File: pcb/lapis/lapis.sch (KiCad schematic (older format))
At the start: 0 parts

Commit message: 基板修正途中　ソフト動作確認まで
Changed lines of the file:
@@
 $EndDescr
 $Sheet
-S 2000 1500 1600 1350
+S 8050 2900 800  650
+U 5FA81E9C
+F0 "IMU" 50
+F1 "ICM-20602.sch" 50
+F2 "IMU_MISO" O L 8050 3450 50
+F3 "IMU_CS" I L 8050 3000 50
+F4 "IMU_MOSI" I L 8050 3300 50
+F5 "IMU_SCK" I L 8050 3150 50
+$EndSheet
+$Sheet
+S 1850 3600 850  200
+U 5FA82034
+F0 "WALL_LED_LFRS" 50
+F1 "wall_led.sch" 50
+F2 "LED_PWM" I R 2700 3700 50
+$EndSheet
+$Sheet
+S 1850 4650 900  200
+U 5FA821A9
+F0 "WALL_SENSOR_RS" 50
+F1 "wall_sensor.sch" 50
+F2 "WALLSENSOR_ADC" O R 2750 4750 50
+$EndSheet
+$Sheet
+S 1850 5100 900  200
+U 5FA82203
+F0 "WALL_SENSOR_RF" 50
+F1 "wall_sensor.sch" 50
+F2 "WALLSENSOR_ADC" O R 2750 5200 50
+$EndSheet
+$Sheet
+S 8050 1800 800  700
+U 5FA81F75
+F0 "MOTOR_DRIVE" 50
+F1 "DRV8835.sch" 50
+F2 "MR_PWM" I L 8050 2100 50
+F3 "ML_PWM" I L 8050 2250 50
+F4 "ML_EN" I L 8050 2400 50
+F5 "MR_EN" I L 8050 1950 50
+$EndSheet
+$Sheet
+S 1850 5550 900  200
+U 5FA82246
+F0 "WALL_SENSOR_LF" 50
+F1 "wall_sensor.sch" 50
+F2 "WALLSENSOR_ADC" O R 2750 5650 50
+$EndSheet
+$Sheet
+S 1850 6000 900  200
+U 5FA82233
+F0 "WALL_SENSOR_LS" 50
+F1 "wall_sensor.sch" 50
+F2 "WALLSENSOR_ADC" O R 2750 6100 50
+$EndSheet
+$Sheet
+S 2050 1500 600  200
 U 5FA819E2
 F0 "POWER" 50
 F1 "power.sch" 50
-$EndSheet
-$Sheet
-S 4200 1500 1450 1350
-U 5FA81D59
-F0 "CPU" 50
-F1 "STM32F405RGT.sch" 50
-$EndSheet
-$Sheet
-S 6150 1500 1450 1350
-U 5FA81E9C
-F0 "IMU" 50
-F1 "MPU6500.sch" 50
-$EndSheet
-$Sheet
-S -2650 1100 1600 1300
-U 5FA82034
-F0 "WALL_LED_LFRS" 50
-F1 "wall_led.sch" 50
-$EndSheet
-$Sheet
-S -2600 3850 1150 1250
+F2 "AD_BATT" O R 2650 1600 50
+$EndSheet
+$Sheet
+S 1850 4000 850  200
 U 5FA82132
 F0 "WALL_LED_LSRF" 50
 F1 "wall_led.sch" 50
-$EndSheet
-$Sheet
-S -4600 7350 1400 1300
+F2 "LED_PWM" I R 2700 4100 50
+$EndSheet
+$Sheet
+S 8050 4150 1000 650
 U 5FA82159
 F0 "MOTOR_ENCODER_R" 50
 F1 "AS5047P.sch" 50
-$EndSheet
-$Sheet
-S -4250 5150 1400 1400
-U 5FA821A9
-F0 "WALL_SENSOR_RS" 50
-F1 "wall_sensor.sch" 50
-$EndSheet
-$Sheet
-S -2250 7400 1250 1350
-U 5FA82203
-F0 "WALL_SENSOR_RF" 50
-F1 "wall_sensor.sch" 50
-$EndSheet
-$Sheet
-S -2150 5550 1400 1000
+F2 "ENC_CS" I L 8050 4250 50
+F3 "ENC_SCK" I L 8050 4400 50
+F4 "ENC_MISO" O L 8050 4700 50
+F5 "ENC_MOSI" I L 8050 4550 50
+$EndSheet
+$Sheet
+S 8050 5250 1000 650
 U 5FA82269
 F0 "MOTOR_ENCODER_L" 50
 F1 "AS5047P.sch" 50
-$EndSheet
-$Sheet
-S 8000 1500 1400 1350
-U 5FA81F75
-F0 "MOTOR_DRIVE" 50
-F1 "DRV8835.sch" 50
-$EndSheet
-$Sheet
-S -2500 2850 850  650
-U 5FA82246
-F0 "WALL_SENSOR_LF" 50
-F1 "wall_sensor.sch" 50
-$EndSheet
-$Sheet
-S -4300 1150 750  650
-U 5FA82233
-F0 "WALL_SENSOR_LS" 50
-F1 "wall_sensor.sch" 50
-$EndSheet
-$Sheet
-S 1500 3850 1500 1600
-U 5FA82AB3
-F0 "INDICATOR" 50
-F1 "indicator.sch" 50
+F2 "ENC_CS" I L 8050 5350 50
+F3 "ENC_SCK" I L 8050 5500 50
+F4 "ENC_MISO" O L 8050 5800 50
+F5 "ENC_MOSI" I L 8050 5650 50
+$EndSheet
+Wire Wire Line
+	2650 1600 4000 1600
+Wire Wire Line
+	2650 2450 4000 2450
+Wire Wire Line
+	2650 2550 4000 2550
+Wire Wire Line
+	4000 2700 2650 2700
+Wire Wire Line
+	2650 2850 4000 2850
+Wire Wire Line
+	4000 2950 2650 2950
+Wire Wire Line
+	2650 3050 4000 3050
+Wire Wire Line
+	4000 3150 2650 3150
+Wire Wire Line
+	4000 3700 2700 3700
+Wire Wire Line
+	2700 4100 4000 4100
+Wire Wire Line
+	4000 4750 2750 4750
+Wire Wire Line
+	2750 5200 4000 5200
+Wire Wire Line
+	4000 5650 2750 5650
+Wire Wire Line
+	2750 6100 4000 6100
+Wire Wire Line
+	8050 1950 7100 1950
+Wire Wire Line
+	8050 2100 7100 2100
+Wire Wire Line
+	7100 2250 8050 2250
+Wire Wire Line
+	8050 2400 7100 2400
+Wire Wire Line
+	7100 3000 8050 3000
+Wire Wire Line
+	8050 3150 7100 3150
+Wire Wire Line
+	7100 3300 8050 3300
+Wire Wire Line
+	7100 3450 8050 3450
+Wire Wire Line
+	8050 4250 7100 4250
+Wire Wire Line
+	7100 4400 7850 4400
+Wire Wire Line
+	8050 4550 7700 4550
+Wire Wire Line
+	7100 4700 7550 4700
+Wire Wire Line
+	8050 5350 7100 5350
+Wire Wire Line
+	7850 4400 7850 5500
+Wire Wire Line
+	7850 5500 8050 5500
+Connection ~ 7850 4400
+Wire Wire Line
+	7850 4400 8050 4400
+Wire Wire Line
+	7700 4550 7700 5650
+Wire Wire Line
+	7700 5650 8050 5650
+Connection ~ 7700 4550
+Wire Wire Line
+	7700 4550 7100 4550
+Wire Wire Line
+	7550 4700 7550 5800
+Wire Wire Line
+	7550 5800 8050 5800
+Connection ~ 7550 4700
+Wire Wire Line
+	7550 4700 8050 4700
+Wire Wire Line
+	2650 2300 4000 2300
+$Sheet
+S 4000 1450 3100 4800
+U 5FA81D59
+F0 "CPU" 50
+F1 "STM32F411CEU.sch" 50
+F2 "LED_LFRS" O L 4000 3700 50
+F3 "LED_LSRF" O L 4000 4100 50
+F4 "MR_PWM" O R 7100 2100 50
+F5 "MR_EN" O R 7100 1950 50
+F6 "ML_PWM" O R 7100 2250 50
+F7 "ML_EN" O R 7100 2400 50
+F8 "ENC_SCK" O R 7100 4400 50
+F9 "ENC_CS_R" O R 7100 4250 50
+F10 "ENC_CS_L" O R 7100 5350 50
+F11 "ENC_MISO" I R 7100 4700 50
+F12 "ENC_MOSI" O R 7100 4550 50
+F13 "WALLSENSOR_RS" I L 4000 4750 50
+F14 "WALLSENSOR_RF" I L 4000 5200 50
+F15 "WALLSENSOR_LF" I L 4000 5650 50
+F16 "WALLSENSOR_LS" I L 4000 6100 50
+F17 "BATTERY" I L 4000 1600 50
+F18 "IMU_SCK" O R 7100 3150 50
+F19 "IMU_MISO" I R 7100 3450 50
+F20 "IMU_MOSI" O R 7100 3300 50
+F21 "IMU_CS" O R 7100 3000 50
+F22 "SW" I L 4000 2700 50
+F23 "LED1" O L 4000 2950 50
+F24 "LED2" O L 4000 3050 50
+F25 "LED3" O L 4000 3150 50
+F26 "RX" I L 4000 2550 50
+F27 "SPEAKER" O L 4000 2300 50
+F28 "TX" O L 4000 2450 50
+F29 "LED0" O L 4000 2850 50
+$EndSheet
+$Sheet
+S 2100 2200 550  1050
+U 603AF16B
+F0 "UI" 50
+F1 "UI.sch" 50
+F2 "LED1" I R 2650 2950 50
+F3 "LED2" I R 2650 3050 50
+F4 "LED3" I R 2650 3150 50
+F5 "LED0" I R 2650 2850 50
+F6 "SW" O R 2650 2700 50
+F7 "SPEAKER" I R 2650 2300 50
+F8 "TX" I R 2650 2450 50
+F9 "RX" O R 2650 2550 50
 $EndSheet
 $EndSCHEMATC

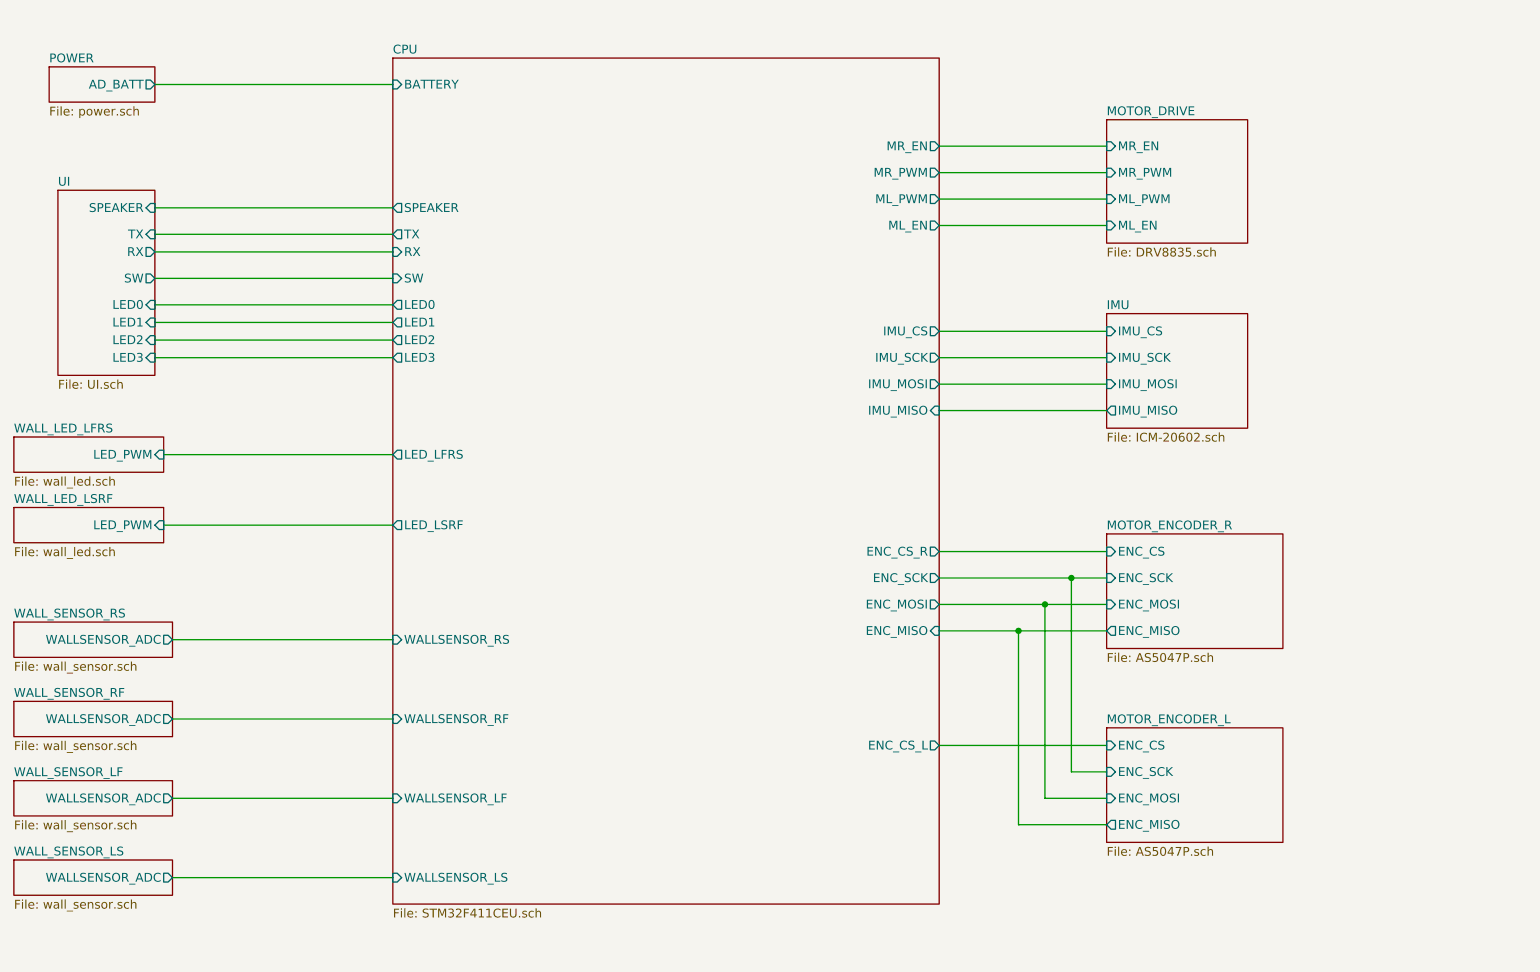
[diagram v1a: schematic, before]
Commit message: 信地旋回探索
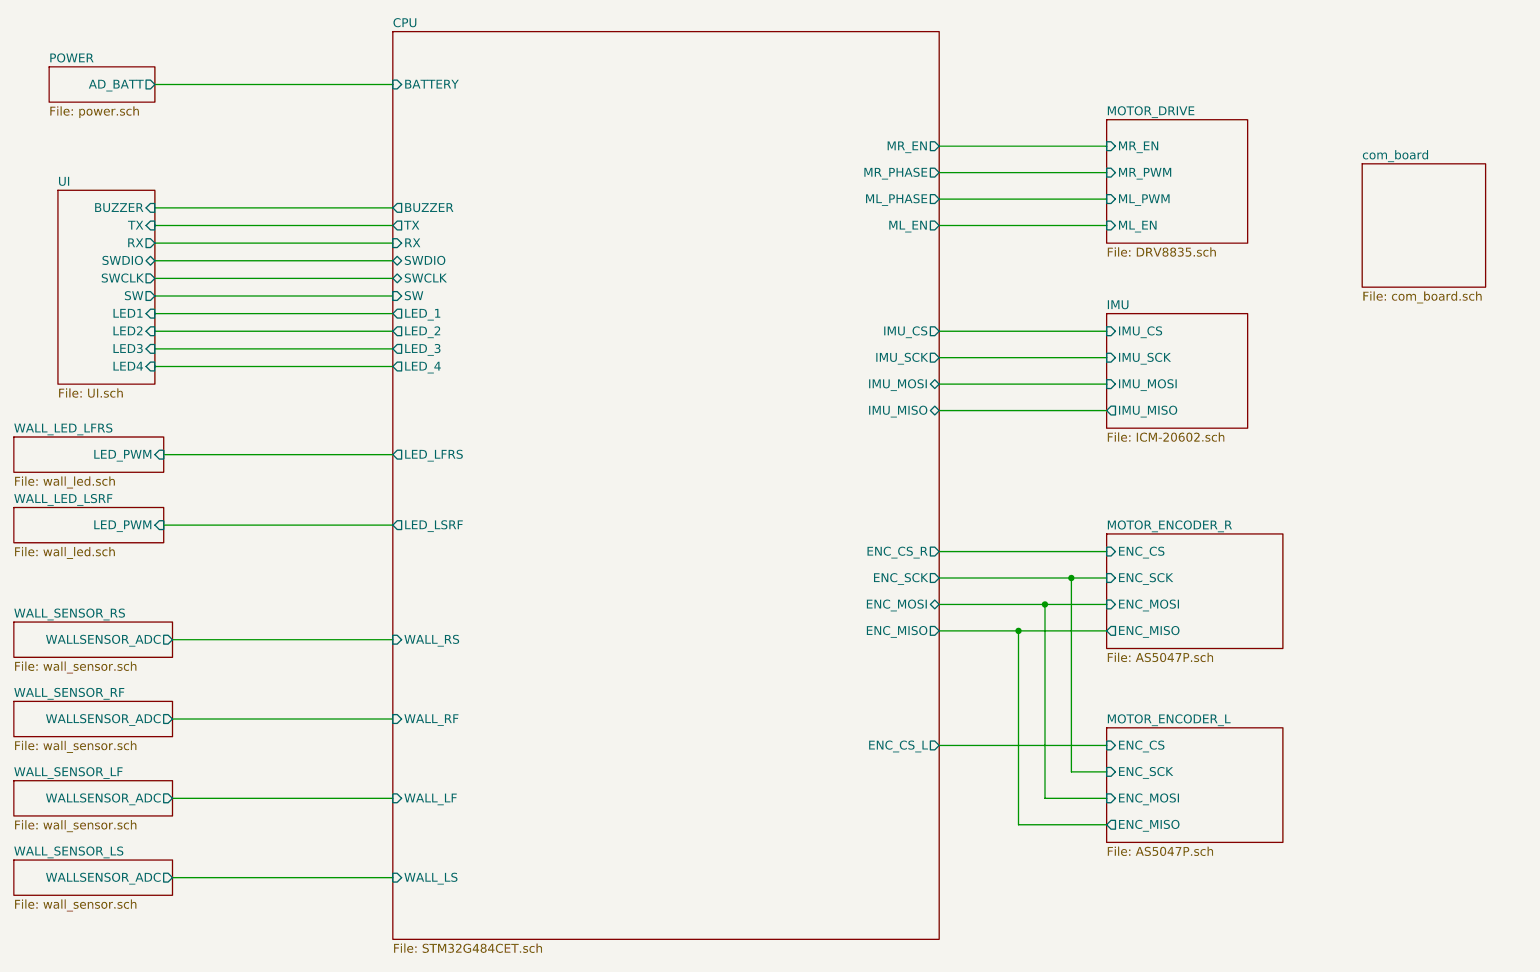
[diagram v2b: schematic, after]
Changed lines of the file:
@@
 $Descr A4 11693 8268
 encoding utf-8
-Sheet 1 14
+Sheet 1 15
 Title ""
 Date ""
@@
 $EndSheet
 $Sheet
-S 1850 3600 850  200
-U 5FA82034
-F0 "WALL_LED_LFRS" 50
-F1 "wall_led.sch" 50
-F2 "LED_PWM" I R 2700 3700 50
-$EndSheet
-$Sheet
-S 1850 4650 900  200
-U 5FA821A9
-F0 "WALL_SENSOR_RS" 50
-F1 "wall_sensor.sch" 50
-F2 "WALLSENSOR_ADC" O R 2750 4750 50
-$EndSheet
-$Sheet
-S 1850 5100 900  200
-U 5FA82203
-F0 "WALL_SENSOR_RF" 50
-F1 "wall_sensor.sch" 50
-F2 "WALLSENSOR_ADC" O R 2750 5200 50
-$EndSheet
-$Sheet
 S 8050 1800 800  700
 U 5FA81F75
@@
 $EndSheet
 $Sheet
-S 1850 5550 900  200
-U 5FA82246
-F0 "WALL_SENSOR_LF" 50
-F1 "wall_sensor.sch" 50
-F2 "WALLSENSOR_ADC" O R 2750 5650 50
-$EndSheet
-$Sheet
-S 1850 6000 900  200
-U 5FA82233
-F0 "WALL_SENSOR_LS" 50
-F1 "wall_sensor.sch" 50
-F2 "WALLSENSOR_ADC" O R 2750 6100 50
-$EndSheet
-$Sheet
 S 2050 1500 600  200
 U 5FA819E2
@@
 F1 "power.sch" 50
 F2 "AD_BATT" O R 2650 1600 50
-$EndSheet
-$Sheet
-S 1850 4000 850  200
-U 5FA82132
-F0 "WALL_LED_LSRF" 50
-F1 "wall_led.sch" 50
-F2 "LED_PWM" I R 2700 4100 50
 $EndSheet
 $Sheet
@@
 	2650 1600 4000 1600
 Wire Wire Line
-	2650 2450 4000 2450
-Wire Wire Line
-	2650 2550 4000 2550
-Wire Wire Line
-	4000 2700 2650 2700
-Wire Wire Line
-	2650 2850 4000 2850
-Wire Wire Line
-	4000 2950 2650 2950
-Wire Wire Line
-	2650 3050 4000 3050
-Wire Wire Line
-	4000 3150 2650 3150
-Wire Wire Line
-	4000 3700 2700 3700
-Wire Wire Line
-	2700 4100 4000 4100
-Wire Wire Line
-	4000 4750 2750 4750
-Wire Wire Line
-	2750 5200 4000 5200
-Wire Wire Line
-	4000 5650 2750 5650
-Wire Wire Line
-	2750 6100 4000 6100
+	4000 2800 2650 2800
+Wire Wire Line
+	2650 2900 4000 2900
+Wire Wire Line
+	4000 3000 2650 3000
+Wire Wire Line
+	2650 3100 4000 3100
+Wire Wire Line
+	4000 3200 2650 3200
 Wire Wire Line
 	8050 1950 7100 1950
@@
 	2650 2300 4000 2300
 $Sheet
-S 4000 1450 3100 4800
-U 5FA81D59
-F0 "CPU" 50
-F1 "STM32F411CEU.sch" 50
-F2 "LED_LFRS" O L 4000 3700 50
-F3 "LED_LSRF" O L 4000 4100 50
-F4 "MR_PWM" O R 7100 2100 50
-F5 "MR_EN" O R 7100 1950 50
-F6 "ML_PWM" O R 7100 2250 50
-F7 "ML_EN" O R 7100 2400 50
-F8 "ENC_SCK" O R 7100 4400 50
-F9 "ENC_CS_R" O R 7100 4250 50
-F10 "ENC_CS_L" O R 7100 5350 50
-F11 "ENC_MISO" I R 7100 4700 50
-F12 "ENC_MOSI" O R 7100 4550 50
-F13 "WALLSENSOR_RS" I L 4000 4750 50
-F14 "WALLSENSOR_RF" I L 4000 5200 50
-F15 "WALLSENSOR_LF" I L 4000 5650 50
-F16 "WALLSENSOR_LS" I L 4000 6100 50
-F17 "BATTERY" I L 4000 1600 50
-F18 "IMU_SCK" O R 7100 3150 50
-F19 "IMU_MISO" I R 7100 3450 50
-F20 "IMU_MOSI" O R 7100 3300 50
-F21 "IMU_CS" O R 7100 3000 50
-F22 "SW" I L 4000 2700 50
-F23 "LED1" O L 4000 2950 50
-F24 "LED2" O L 4000 3050 50
-F25 "LED3" O L 4000 3150 50
-F26 "RX" I L 4000 2550 50
-F27 "SPEAKER" O L 4000 2300 50
-F28 "TX" O L 4000 2450 50
-F29 "LED0" O L 4000 2850 50
-$EndSheet
-$Sheet
-S 2100 2200 550  1050
+S 2100 2200 550  1100
 U 603AF16B
 F0 "UI" 50
 F1 "UI.sch" 50
-F2 "LED1" I R 2650 2950 50
-F3 "LED2" I R 2650 3050 50
-F4 "LED3" I R 2650 3150 50
-F5 "LED0" I R 2650 2850 50
-F6 "SW" O R 2650 2700 50
-F7 "SPEAKER" I R 2650 2300 50
-F8 "TX" I R 2650 2450 50
-F9 "RX" O R 2650 2550 50
+F2 "TX" I R 2650 2400 50
+F3 "RX" O R 2650 2500 50
+F4 "SWDIO" B R 2650 2600 50
+F5 "SWCLK" O R 2650 2700 50
+F6 "SW" O R 2650 2800 50
+F7 "BUZZER" I R 2650 2300 50
+F8 "LED4" I R 2650 3200 50
+F9 "LED3" I R 2650 3100 50
+F10 "LED2" I R 2650 3000 50
+F11 "LED1" I R 2650 2900 50
+$EndSheet
+Wire Wire Line
+	2750 6100 4000 6100
+Wire Wire Line
+	4000 5650 2750 5650
+Wire Wire Line
+	2750 5200 4000 5200
+Wire Wire Line
+	4000 4750 2750 4750
+Wire Wire Line
+	2700 4100 4000 4100
+Wire Wire Line
+	4000 3700 2700 3700
+$Sheet
+S 1850 4000 850  200
+U 5FA82132
+F0 "WALL_LED_LSRF" 50
+F1 "wall_led.sch" 50
+F2 "LED_PWM" I R 2700 4100 50
+$EndSheet
+$Sheet
+S 1850 6000 900  200
+U 5FA82233
+F0 "WALL_SENSOR_LS" 50
+F1 "wall_sensor.sch" 50
+F2 "WALLSENSOR_ADC" O R 2750 6100 50
+$EndSheet
+$Sheet
+S 1850 5550 900  200
+U 5FA82246
+F0 "WALL_SENSOR_LF" 50
+F1 "wall_sensor.sch" 50
+F2 "WALLSENSOR_ADC" O R 2750 5650 50
+$EndSheet
+$Sheet
+S 1850 5100 900  200
+U 5FA82203
+F0 "WALL_SENSOR_RF" 50
+F1 "wall_sensor.sch" 50
+F2 "WALLSENSOR_ADC" O R 2750 5200 50
+$EndSheet
+$Sheet
+S 1850 4650 900  200
+U 5FA821A9
+F0 "WALL_SENSOR_RS" 50
+F1 "wall_sensor.sch" 50
+F2 "WALLSENSOR_ADC" O R 2750 4750 50
+$EndSheet
+$Sheet
+S 1850 3600 850  200
+U 5FA82034
+F0 "WALL_LED_LFRS" 50
+F1 "wall_led.sch" 50
+F2 "LED_PWM" I R 2700 3700 50
+$EndSheet
+Wire Wire Line
+	2650 2400 4000 2400
+Wire Wire Line
+	4000 2500 2650 2500
+Wire Wire Line
+	2650 2600 4000 2600
+Wire Wire Line
+	4000 2700 2650 2700
+$Sheet
+S 9500 2050 700  700
+U 61A6221A
+F0 "com_board" 50
+F1 "com_board.sch" 50
+$EndSheet
+$Sheet
+S 4000 1300 3100 5150
+U 618DADBF
+F0 "CPU" 50
+F1 "STM32G484CET.sch" 50
+F2 "SWDIO" B L 4000 2600 50
+F3 "SWCLK" B L 4000 2700 50
+F4 "SW" I L 4000 2800 50
+F5 "RX" I L 4000 2500 50
+F6 "LED_LFRS" O L 4000 3700 50
+F7 "ML_EN" O R 7100 2400 50
+F8 "MR_EN" O R 7100 1950 50
+F9 "ENC_MISO" O R 7100 4700 50
+F10 "TX" O L 4000 2400 50
+F11 "ENC_CS_R" O R 7100 4250 50
+F12 "ENC_MOSI" B R 7100 4550 50
+F13 "BATTERY" I L 4000 1600 50
+F14 "BUZZER" O L 4000 2300 50
+F15 "MR_PHASE" O R 7100 2100 50
+F16 "ML_PHASE" O R 7100 2250 50
+F17 "IMU_CS" O R 7100 3000 50
+F18 "IMU_MOSI" B R 7100 3300 50
+F19 "IMU_MISO" B R 7100 3450 50
+F20 "IMU_SCK" O R 7100 3150 50
+F21 "ENC_CS_L" O R 7100 5350 50
+F22 "WALL_LS" I L 4000 6100 50
+F23 "WALL_LF" I L 4000 5650 50
+F24 "WALL_RF" I L 4000 5200 50
+F25 "WALL_RS" I L 4000 4750 50
+F26 "ENC_SCK" O R 7100 4400 50
+F27 "LED_4" O L 4000 3200 50
+F28 "LED_3" O L 4000 3100 50
+F29 "LED_2" O L 4000 3000 50
+F30 "LED_1" O L 4000 2900 50
+F31 "LED_LSRF" O L 4000 4100 50
 $EndSheet
 $EndSCHEMATC
